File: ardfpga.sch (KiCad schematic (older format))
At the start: 52 parts, among them J1 AD, J2 PWR, J3 ICSP, Q1 NMOS, Q2 NMOS, U1 iCE40LP384, U2 AT25xxx, U3 ATMega328, U4 CH340G, X1 16MHz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

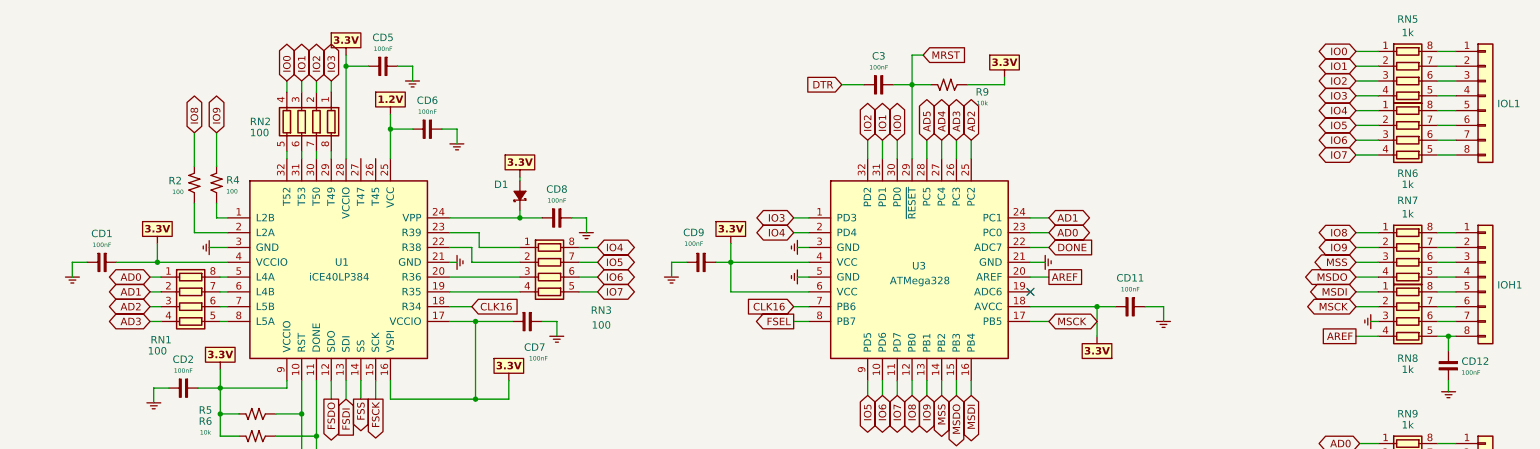
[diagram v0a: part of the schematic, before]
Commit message: Board routed, circuit changed to ease PCB routing. Minor adjustments. Ready to re-check PCB.
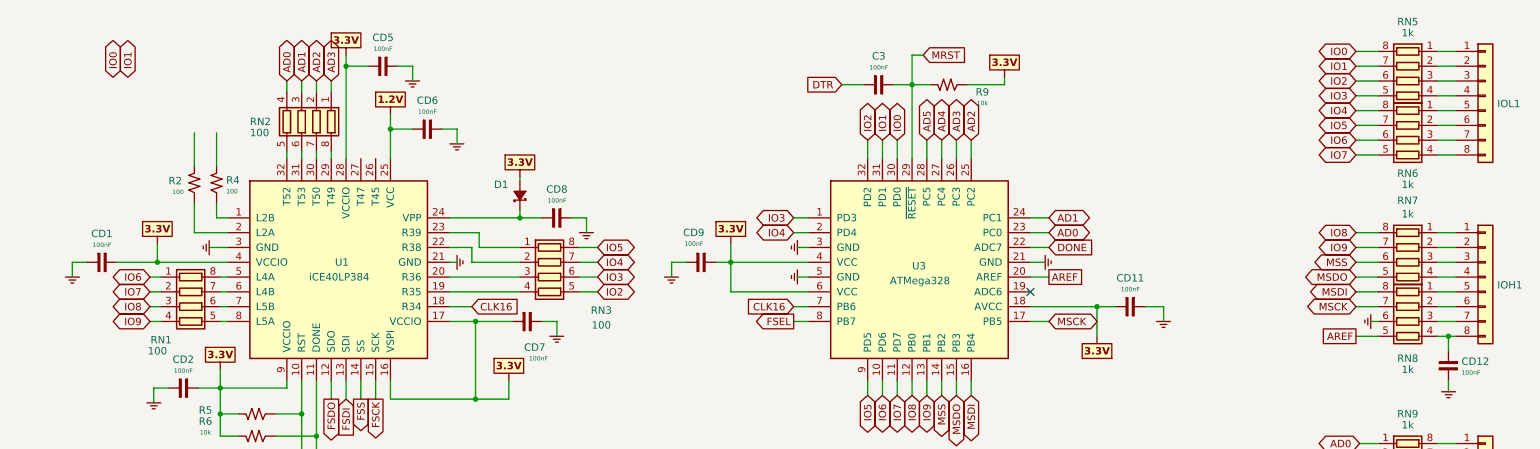
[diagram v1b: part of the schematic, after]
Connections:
- net AD0: now also RN2.4 (R4.1); no longer RN1.1 (R1.1)
- net AD1: now also RN2.3 (R3.1); no longer RN1.2 (R2.1)
- net AD2: now also RN2.2 (R2.1); no longer RN1.3 (R3.1)
- net AD3: now also RN2.1 (R1.1); no longer RN1.4 (R4.1)
- net AREF: now also RN8.5 (R4.2); no longer RN8.4 (R4.1)
- net GND: now also RN8.6 (R3.2); no longer RN8.3 (R3.1)
- net IO0: now also RN5.8 (R1.2); no longer RN2.4 (R4.1), RN5.1 (R1.1)
- net IO1: now also RN5.7 (R2.2); no longer RN2.3 (R3.1), RN5.2 (R2.1)
- net IO2: now also RN3.5 (R4.2), RN5.6 (R3.2); no longer RN2.2 (R2.1), RN5.3 (R3.1)
- net IO3: now also RN3.6 (R3.2), RN5.5 (R4.2); no longer RN2.1 (R1.1), RN5.4 (R4.1)
- net IO4: now also RN3.7 (R2.2), RN6.8 (R1.2); no longer RN3.8 (R1.2), RN6.1 (R1.1)
- net IO5: now also RN3.8 (R1.2), RN6.7 (R2.2); no longer RN3.7 (R2.2), RN6.2 (R2.1)
- net IO6: now also RN1.1 (R1.1), RN6.6 (R3.2); no longer RN3.6 (R3.2), RN6.3 (R3.1)
- net IO7: now also RN1.2 (R2.1), RN6.5 (R4.2); no longer RN3.5 (R4.2), RN6.4 (R4.1)
- net IO8: now also RN1.3 (R3.1), RN7.8 (R1.2); no longer R2.1, RN7.1 (R1.1)
- net IO9: now also RN1.4 (R4.1), RN7.7 (R2.2); no longer R4.1, RN7.2 (R2.1)
- net MSCK: now also RN8.7 (R2.2); no longer RN8.2 (R2.1)
- net MSDI: now also RN8.8 (R1.2); no longer RN8.1 (R1.1)
- net MSDO: now also RN7.5 (R4.2); no longer RN7.4 (R4.1)
- net MSS: now also RN7.6 (R3.2); no longer RN7.3 (R3.1)
- net at IOL1.1 (Pin_1): now also RN5.1 (R1.1); no longer RN5.8 (R1.2)
- net at IOL1.2 (Pin_2): now also RN5.2 (R2.1); no longer RN5.7 (R2.2)
- net at IOL1.3 (Pin_3): now also RN5.3 (R3.1); no longer RN5.6 (R3.2)
- net at IOL1.4 (Pin_4): now also RN5.4 (R4.1); no longer RN5.5 (R4.2)
- net at IOL1.5 (Pin_5): now also RN6.1 (R1.1); no longer RN6.8 (R1.2)
- net at IOL1.6 (Pin_6): now also RN6.2 (R2.1); no longer RN6.7 (R2.2)
- net at IOL1.7 (Pin_7): now also RN6.3 (R3.1); no longer RN6.6 (R3.2)
- net at IOL1.8 (Pin_8): now also RN6.4 (R4.1); no longer RN6.5 (R4.2)
- net at IOH1.1 (Pin_1): now also RN7.1 (R1.1); no longer RN7.8 (R1.2)
- net at IOH1.2 (Pin_2): now also RN7.2 (R2.1); no longer RN7.7 (R2.2)
- net at IOH1.3 (Pin_3): now also RN7.3 (R3.1); no longer RN7.6 (R3.2)
- net at IOH1.4 (Pin_4): now also RN7.4 (R4.1); no longer RN7.5 (R4.2)
- net at IOH1.5 (Pin_5): now also RN8.1 (R1.1); no longer RN8.8 (R1.2)
- net at IOH1.6 (Pin_6): now also RN8.2 (R2.1); no longer RN8.7 (R2.2)
- net at IOH1.7 (Pin_7): now also RN8.3 (R3.1); no longer RN8.6 (R3.2)
- net at CD12.1, IOH1.8 (Pin_8): now also RN8.4 (R4.1); no longer RN8.5 (R4.2)
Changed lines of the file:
@@
 U 1 1 6021EBB2
 P 10100 1050
-F 0 "RN5" V 9683 1050 50  0000 C CNN
-F 1 "1k" V 9774 1050 50  0000 C CNN
+F 0 "RN5" V 9700 1050 50  0000 C CNN
+F 1 "1k" V 9775 1050 50  0000 C CNN
 F 2 "Resistor_SMD:R_Array_Concave_4x0603" V 10375 1050 50  0001 C CNN
 F 3 "~" H 10100 1050 50  0001 C CNN
 	1    10100 1050
-	0    1    1    0
+	0    -1   1    0
 $EndComp
 $Comp
@@
 F 3 "~" H 10100 1450 50  0001 C CNN
 	1    10100 1450
-	0    1    1    0
+	0    -1   1    0
 $EndComp
 Wire Wire Line
@@
 F 3 "~" H 10100 2275 50  0001 C CNN
 	1    10100 2275
-	0    1    1    0
+	0    -1   1    0
 $EndComp
 $Comp
@@
 F 3 "~" H 10100 2675 50  0001 C CNN
 	1    10100 2675
-	0    1    1    0
+	0    -1   1    0
 $EndComp
 Wire Wire Line
@@
 Wire Wire Line
 	3825 6375 3650 6375
-Text GLabel 2525 1050 1    50   BiDi ~ 0
+Text GLabel 1350 1025 1    50   BiDi ~ 0
 IO0
-Text GLabel 2625 1050 1    50   BiDi ~ 0
+Text GLabel 1450 1025 1    50   BiDi ~ 0
 IO1
-Text GLabel 2725 1050 1    50   BiDi ~ 0
+Text GLabel 4625 2475 2    50   BiDi ~ 0
 IO2
-Text GLabel 2825 1050 1    50   BiDi ~ 0
+Text GLabel 4625 2375 2    50   BiDi ~ 0
 IO3
 Wire Wire Line
@@
 Wire Wire Line
 	2825 1050 2825 1125
+Text GLabel 4625 2275 2    50   BiDi ~ 0
+IO4
 Text GLabel 4625 2175 2    50   BiDi ~ 0
-IO4
-Text GLabel 4625 2275 2    50   BiDi ~ 0
 IO5
-Text GLabel 4625 2375 2    50   BiDi ~ 0
+Text GLabel 1600 2375 0    50   BiDi ~ 0
 IO6
-Text GLabel 4625 2475 2    50   BiDi ~ 0
+Text GLabel 1600 2475 0    50   BiDi ~ 0
 IO7
 Wire Wire Line
@@
 Wire Wire Line
 	2075 2675 2125 2675
-Text GLabel 1600 2375 0    50   BiDi ~ 0
+Text GLabel 2525 1050 1    50   BiDi ~ 0
 AD0
-Text GLabel 1600 2475 0    50   BiDi ~ 0
+Text GLabel 2625 1050 1    50   BiDi ~ 0
 AD1
-Text GLabel 1600 2575 0    50   BiDi ~ 0
+Text GLabel 2725 1050 1    50   BiDi ~ 0
 AD2
-Text GLabel 1600 2675 0    50   BiDi ~ 0
+Text GLabel 2825 1050 1    50   BiDi ~ 0
 AD3
 Wire Wire Line
@@
 Wire Wire Line
 	1900 2075 2125 2075
-Text GLabel 1900 1400 1    50   BiDi ~ 0
+Text GLabel 1600 2575 0    50   BiDi ~ 0
 IO8
-Text GLabel 2050 1400 1    50   BiDi ~ 0
+Text GLabel 1600 2675 0    50   BiDi ~ 0
 IO9
 Wire Wire Line

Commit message: Board revision, leds added. Better routing.
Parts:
- added D4, D5: LED_Small_ALT, mylib:0603_LED, symbol Device:LED_Small_ALT
- added R14, R15: 220, mylib:0603_RES, symbol OPENMIND:RESS
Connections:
- wire segments 269 -> 278
- no-connect marks 9 -> 11
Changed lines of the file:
@@
 Wire Wire Line
 	3825 6375 3650 6375
-Text GLabel 1350 1025 1    50   BiDi ~ 0
+Text GLabel 1900 1400 1    50   BiDi ~ 0
 IO0
-Text GLabel 1450 1025 1    50   BiDi ~ 0
+Text GLabel 2050 1400 1    50   BiDi ~ 0
 IO1
 Text GLabel 4625 2475 2    50   BiDi ~ 0
@@
 F1 "power.sch" 50
 $EndSheet
+$Comp
+L OPENMIND:RESS R14
+U 1 1 60AC1C46
+P 7700 5950
+F 0 "R14" H 7650 5725 50  0000 L CNN
+F 1 "220" H 7675 5875 30  0000 L CNN
+F 2 "mylib:0603_RES" H 7700 5950 60  0001 C CNN
+F 3 "" H 7700 5950 60  0000 C CNN
+	1    7700 5950
+	-1   0    0    1
+$EndComp
+$Comp
+L Device:LED_Small_ALT D4
+U 1 1 60AC23E1
+P 8000 5950
+F 0 "D4" H 8000 6075 50  0000 C CNN
+F 1 "LED_Small_ALT" H 8000 5836 50  0001 C CNN
+F 2 "mylib:0603_LED" V 8000 5950 50  0001 C CNN
+F 3 "~" V 8000 5950 50  0001 C CNN
+	1    8000 5950
+	-1   0    0    -1
+$EndComp
+$Comp
+L OPENMIND:GND2 #PWR0101
+U 1 1 60AFE19C
+P 8200 6250
+F 0 "#PWR0101" H 8200 6350 30  0001 C CNN
+F 1 "GND2" H 8200 6180 30  0001 C CNN
+F 2 "" H 8200 6250 60  0000 C CNN
+F 3 "" H 8200 6250 60  0000 C CNN
+	1    8200 6250
+	1    0    0    -1
+$EndComp
+Wire Wire Line
+	7800 5950 7900 5950
+$Comp
+L OPENMIND:RESS R15
+U 1 1 60B1240D
+P 7700 6125
+F 0 "R15" H 7650 5800 50  0000 L CNN
+F 1 "220" H 7675 6225 30  0001 L CNN
+F 2 "mylib:0603_RES" H 7700 6125 60  0001 C CNN
+F 3 "" H 7700 6125 60  0000 C CNN
+	1    7700 6125
+	-1   0    0    1
+$EndComp
+$Comp
+L Device:LED_Small_ALT D5
+U 1 1 60B12414
+P 8000 6125
+F 0 "D5" H 8000 6025 50  0000 C CNN
+F 1 "LED_Small_ALT" H 8000 6011 50  0001 C CNN
+F 2 "mylib:0603_LED" V 8000 6125 50  0001 C CNN
+F 3 "~" V 8000 6125 50  0001 C CNN
+	1    8000 6125
+	-1   0    0    -1
+$EndComp
+Wire Wire Line
+	7800 6125 7900 6125
+Wire Wire Line
+	8100 5950 8200 5950
+Wire Wire Line
+	8200 5950 8200 6125
+Wire Wire Line
+	8100 6125 8200 6125
+Connection ~ 8200 6125
+Wire Wire Line
+	8200 6125 8200 6250
+$Comp
+L OPENMIND:+3.3V #PWR0102
+U 1 1 60B4FC1F
+P 7400 5875
+F 0 "#PWR0102" H 7400 6125 30  0001 C CNN
+F 1 "+3.3V" H 7400 6075 30  0001 C CNN
+F 2 "" H 7400 5875 60  0000 C CNN
+F 3 "" H 7400 5875 60  0000 C CNN
+	1    7400 5875
+	1    0    0    -1
+$EndComp
+Wire Wire Line
+	7400 5875 7400 5950
+Wire Wire Line
+	7400 5950 7550 5950
+Text GLabel 7450 6125 0    50   BiDi ~ 0
+MSCK
+Wire Wire Line
+	7450 6125 7550 6125
+NoConn ~ 3025 1575
+NoConn ~ 3125 1575
 $EndSCHEMATC

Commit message: Bugs in the board corrected. Better routing. First BOM version.
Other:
- note added: "* Crystal not needed in some chips"
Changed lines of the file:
@@
 Wire Wire Line
 	4825 4650 4750 4650
+Text GLabel 4825 4850 2    50   BiDi ~ 0
+MSDI
+Wire Wire Line
+	4825 4750 4750 4750
 Text GLabel 4825 4750 2    50   BiDi ~ 0
-MSDI
-Wire Wire Line
-	4825 4750 4750 4750
-Text GLabel 4825 4850 2    50   BiDi ~ 0
 MSDO
 Wire Wire Line
@@
 NoConn ~ 3025 1575
 NoConn ~ 3125 1575
+Text Notes 5700 5450 0    30   ~ 0
+* Crystal not needed in some chips
 $EndSCHEMATC
